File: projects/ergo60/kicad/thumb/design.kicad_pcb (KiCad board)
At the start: 2 copper layers, 48.3 x 47 mm, 24 parts, among them P1 CONN_1, P2 CONN_6, P3 CONN_1, P4 CONN_1, SW1 SW_20, SW10 SW_10, SW11 SW_21, SW15 SW_20, SW2 SW_01, SW3 SW_21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

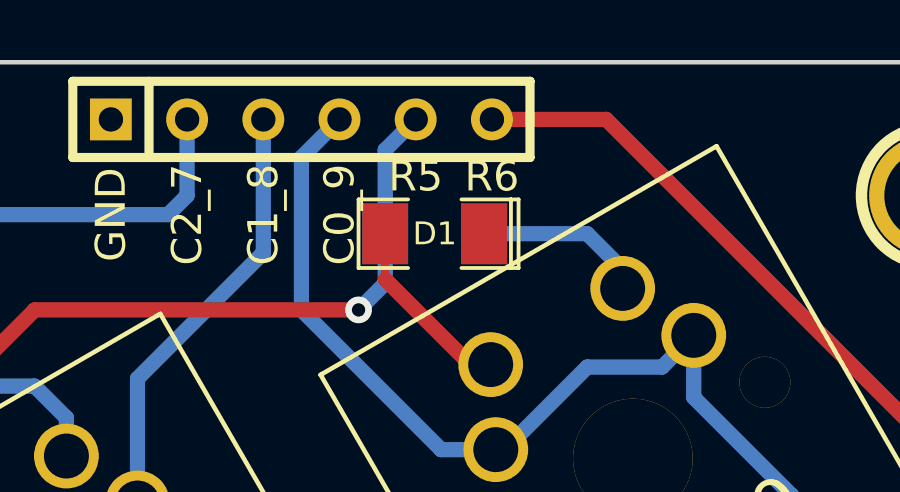
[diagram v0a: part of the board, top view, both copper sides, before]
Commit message: fixing bug in thumb board
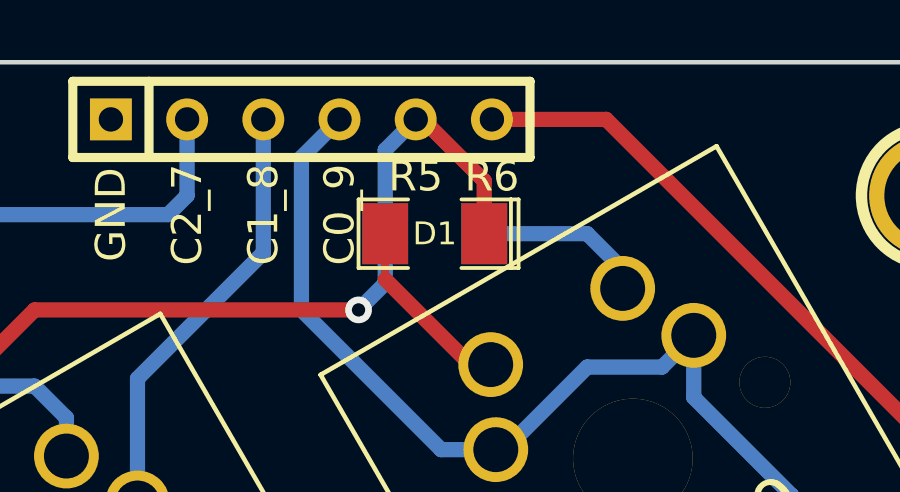
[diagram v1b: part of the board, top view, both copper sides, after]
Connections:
- D1 pad 1: (no net) -> R0
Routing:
- net R0: track 28.2 -> 33.1 mm
